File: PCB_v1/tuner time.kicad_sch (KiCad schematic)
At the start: 15 parts

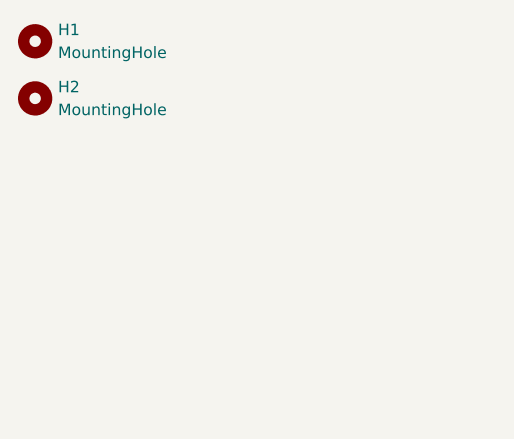
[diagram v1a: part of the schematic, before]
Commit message: added the oscilator
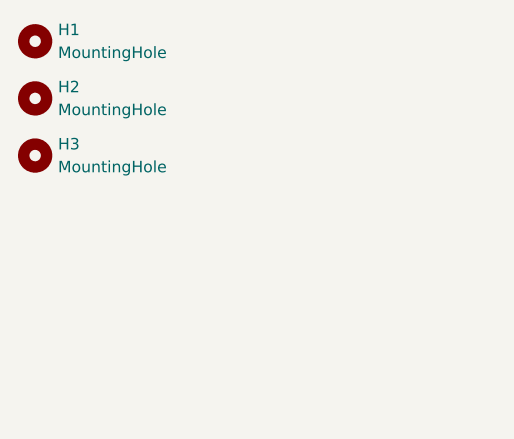
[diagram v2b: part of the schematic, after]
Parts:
- added H3: MountingHole, MountingHole:MountingHole_2.2mm_M2_DIN965_Pad_TopOnly, symbol GT_LIbrary:MountingHole
- D1, D2, D3: footprint LED_SMD:LED_0805_2012Metric_Pad1.15x1.40mm_HandSolder -> LED_0805_2012Metric_Pad1.15x1.40mm_HandSolder
- TP1, TP2: footprint TestPoint:TestPoint_THTPad_D1.0mm_Drill0.5mm -> TestPoint_THTPad_D0.5mm_Drill0.3mm
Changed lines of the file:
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@@
 			)
 		)
-		(property "Footprint" "TestPoint:TestPoint_THTPad_D1.0mm_Drill0.5mm"
+		(property "Footprint" "TestPoint_THTPad_D0.5mm_Drill0.3mm"
 			(at 232.41 81.28 0)
 			(effects
@@
 			)
 		)
-		(property "Footprint" "LED_SMD:LED_0805_2012Metric_Pad1.15x1.40mm_HandSolder"
+		(property "Footprint" "LED_0805_2012Metric_Pad1.15x1.40mm_HandSolder"
 			(at 133.35 24.13 0)
 			(effects
@@
 			)
 		)
-		(property "Footprint" "LED_SMD:LED_0805_2012Metric_Pad1.15x1.40mm_HandSolder"
+		(property "Footprint" "LED_0805_2012Metric_Pad1.15x1.40mm_HandSolder"
 			(at 133.35 33.02 0)
 			(effects
@@
 	)
 	(symbol
+		(lib_id "GT_LIbrary:MountingHole")
+		(at 19.05 30.48 0)
+		(unit 1)
+		(exclude_from_sim yes)
+		(in_bom no)
+		(on_board yes)
+		(dnp no)
+		(fields_autoplaced yes)
+		(property "Reference" "H3"
+			(at 21.59 29.2099 0)
+			(effects
+				(font
+					(size 1.27 1.27)
+				)
+				(justify left)
+			)
+		)
+		(property "Value" "MountingHole"
+			(at 21.59 31.7499 0)
+			(effects
+				(font
+					(size 1.27 1.27)
+				)
+				(justify left)
+			)
+		)
+		(property "Footprint" "MountingHole:MountingHole_2.2mm_M2_DIN965_Pad_TopOnly"
+			(at 19.05 30.48 0)
+			(effects
+				(font
+					(size 1.27 1.27)
+				)
+				(hide yes)
+			)
+		)
+		(property "Datasheet" "~"
+			(at 19.05 30.48 0)
+			(effects
+				(font
+					(size 1.27 1.27)
+				)
+				(hide yes)
+			)
+		)
+		(property "Description" "Mounting Hole without connection"
+			(at 19.05 30.48 0)
+			(effects
+				(font
+					(size 1.27 1.27)
+				)
+				(hide yes)
+			)
+		)
+		(property "MFP" "N/A"
+			(at 19.05 30.48 0)
+			(effects
+				(font
+					(size 1.27 1.27)
+				)
+				(hide yes)
+			)
+		)
+		(instances
+			(project "tuner time"
+				(path "/353cef6a-fb6e-40d9-89f8-eb54b7aa5118"
+					(reference "H3")
+					(unit 1)
+				)
+			)
+		)
+	)
+	(symbol
 		(lib_id "GT_LIbrary:VCC")
 		(at 176.53 76.2 0)
@@
 			)
 		)
-		(property "Footprint" "LED_SMD:LED_0805_2012Metric_Pad1.15x1.40mm_HandSolder"
+		(property "Footprint" "LED_0805_2012Metric_Pad1.15x1.40mm_HandSolder"
 			(at 224.79 97.79 0)
 			(effects
@@
 			)
 		)
-		(property "Footprint" "TestPoint:TestPoint_THTPad_D1.0mm_Drill0.5mm"
+		(property "Footprint" "TestPoint_THTPad_D0.5mm_Drill0.3mm"
 			(at 199.39 74.93 0)
 			(effects

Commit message: before major move
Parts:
- removed D3: Green, LED_0805_2012Metric_Pad1.15x1.40mm_HandSolder, symbol GT_LIbrary:LED
- removed JP2: M1, Jumper:SolderJumper-3_P1.3mm_Open_RoundedPad1.0x1.5mm, symbol GT_LIbrary:SolderJumper_3_Open
- removed JP3: M2, Jumper:SolderJumper-3_P1.3mm_Open_RoundedPad1.0x1.5mm, symbol GT_LIbrary:SolderJumper_3_Open
- removed JP4: SLP, Jumper:SolderJumper-3_P1.3mm_Bridged12_RoundedPad1.0x1.5mm, symbol GT_LIbrary:SolderJumper_3_Bridged12
- removed R3: 680, Resistor_SMD:R_0805_2012Metric, symbol GT_LIbrary:R_US
- removed TP1, TP2: ~, TestPoint_THTPad_D0.5mm_Drill0.3mm, symbol GT_LIbrary:TestPoint
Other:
- sheet Motor ports: added Vconfig; removed EN, FLT, M0, M1, SLP, VINT, VREF

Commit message: Placement done
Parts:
- added D3: Green, LED_0805_2012Metric_Pad1.15x1.40mm_HandSolder, symbol GT_LIbrary:LED
- added R3: 680, Resistor_SMD:R_0805_2012Metric, symbol GT_LIbrary:R_US
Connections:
- net GND: now also R3.2
- new net: D3.1 (K), R3.1
- new net Motor/FLT: D3.2 (A)
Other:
- sheet Motor ports: added FLT; removed none

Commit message: before DRC
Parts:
- added TP1: ~, TestPoint_THTPad_D0.8mm_Drill0.4mm, symbol GT_LIbrary:TestPoint
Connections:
- new net Motor/Vconfig: TP1.1

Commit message: done no text before stiching via
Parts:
- R1, R2, R3: footprint Resistor_SMD:R_0805_2012Metric -> Library:R_0805_2012Metric
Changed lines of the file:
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@@
 			)
 		)
-		(property "Footprint" "Resistor_SMD:R_0805_2012Metric"
+		(property "Footprint" "Library:R_0805_2012Metric"
 			(at 123.19 25.908 90)
 			(effects
@@
 			)
 		)
-		(property "Footprint" "Resistor_SMD:R_0805_2012Metric"
+		(property "Footprint" "Library:R_0805_2012Metric"
 			(at 123.19 34.798 90)
 			(effects
@@
 			)
 		)
-		(property "Footprint" "Resistor_SMD:R_0805_2012Metric"
+		(property "Footprint" "Library:R_0805_2012Metric"
 			(at 232.664 95.504 90)
 			(effects
